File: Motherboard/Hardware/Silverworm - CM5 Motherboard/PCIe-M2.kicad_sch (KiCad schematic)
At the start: 24 parts, among them J4 Bus_M.2_Socket_M, M1 M.2 Screw, M2 M.2 Solder Nut, M3 M.2 Solder Nut, M4 M.2 Solder Nut, M5 M.2 Solder Nut, U7 ASEK-32.768KHZ-L-R-T, U8 AP3441SHE-7B

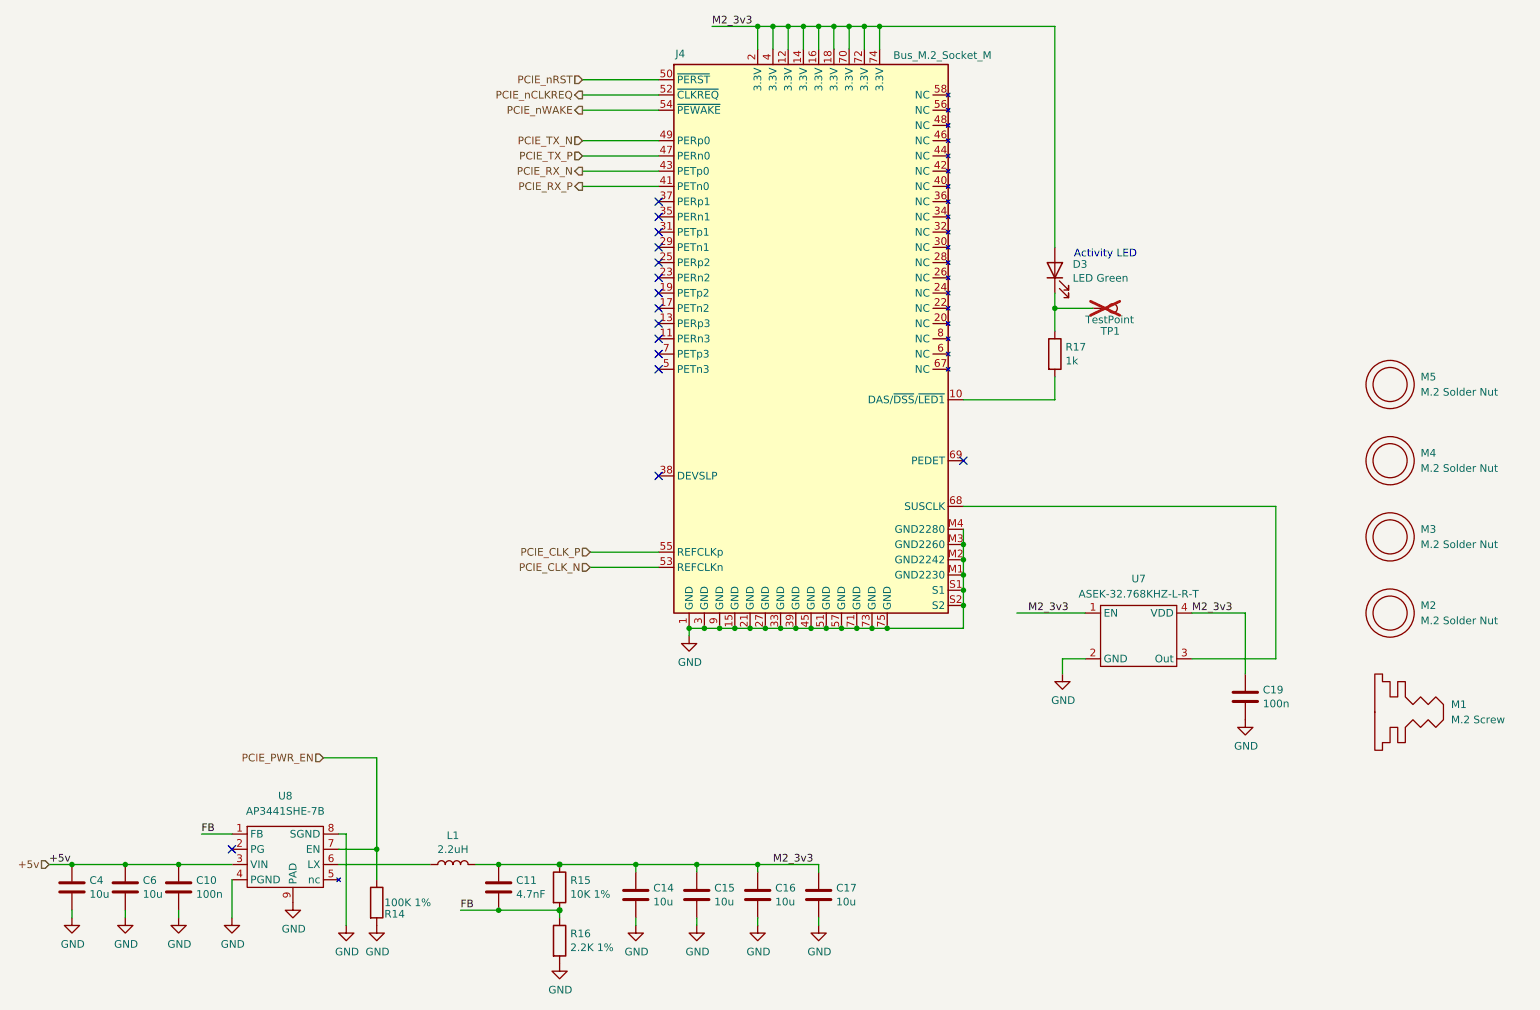
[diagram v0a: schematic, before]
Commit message: Added footprints and board connectors
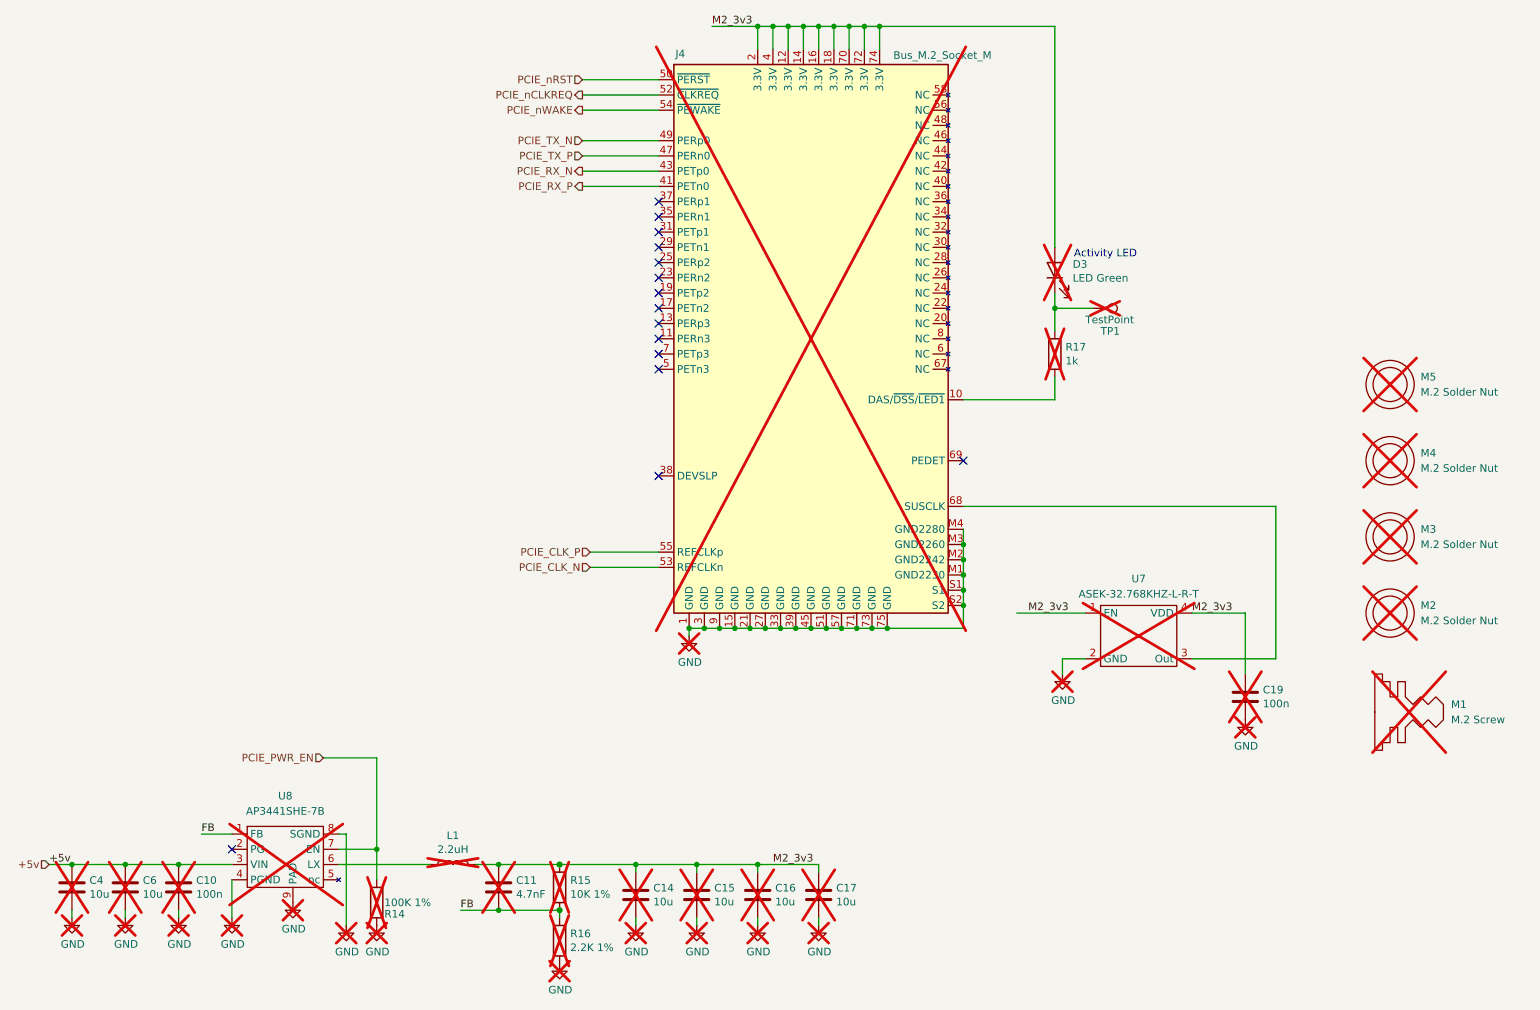
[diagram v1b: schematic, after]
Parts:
- C10, C11, C14, C15, C16, C17, C19, C4, C6, D3, J4, L1, M1, M2, M3, M4, M5, R14, R15, R16, R17, U7, U8: now not fitted; now left out of the parts list

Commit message: PCB changes (many)
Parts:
- renumbered C4 to C10, C6 to C11, C10 to C12, C11 to C13, C19 to C18, J4 to J19, M5 to M1, M4 to M2, M2 to M4, M1 to M5, R14 to R20, R15 to R21, R16 to R22, R17 to R23, TP1 to TP5, U8 to U6
